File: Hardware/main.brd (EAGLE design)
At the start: 100 x 49.2 mm, 40 parts, among them IC3 MEGA128-A, K1 DS2-L2-12V, T1 IRML5202, T2 IRML5202, T3 IRML5202, T4 IRML5202, U1 DS1307ZN+

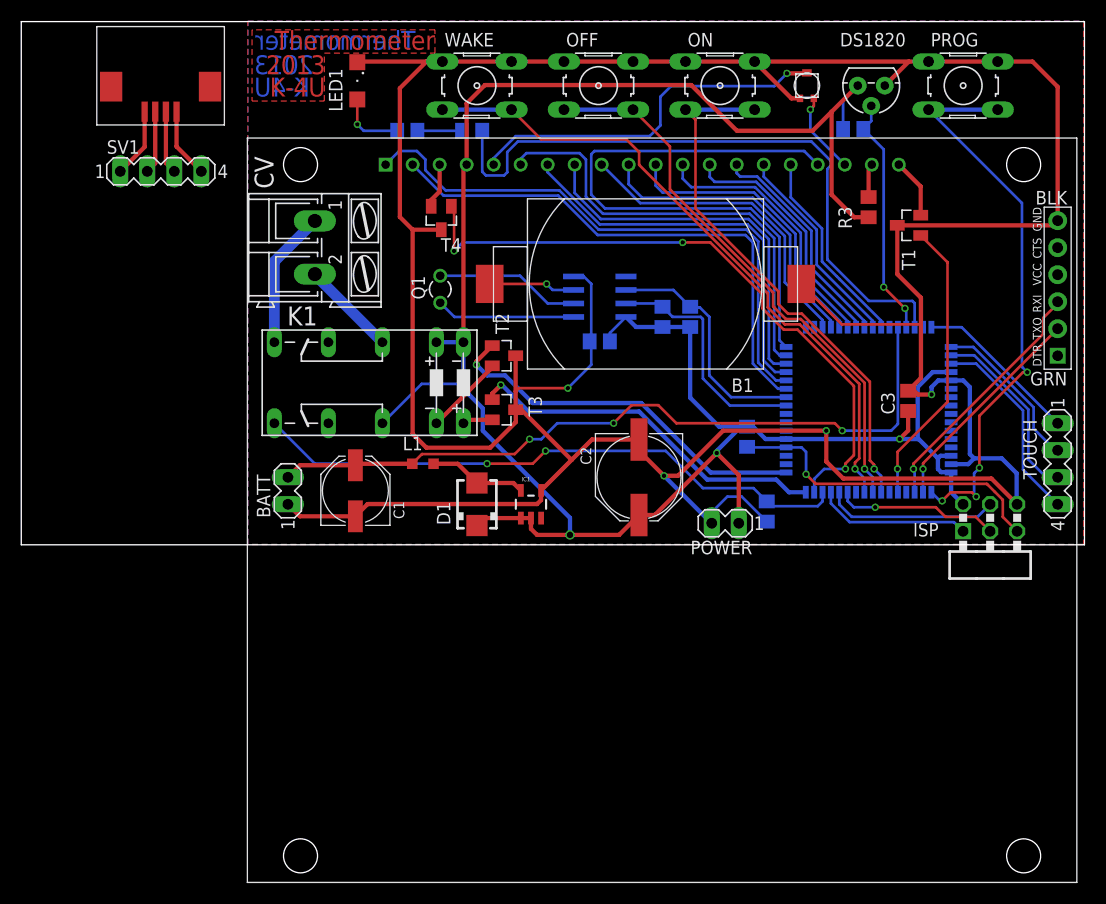
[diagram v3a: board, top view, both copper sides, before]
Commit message: Presets added, time added, CV added
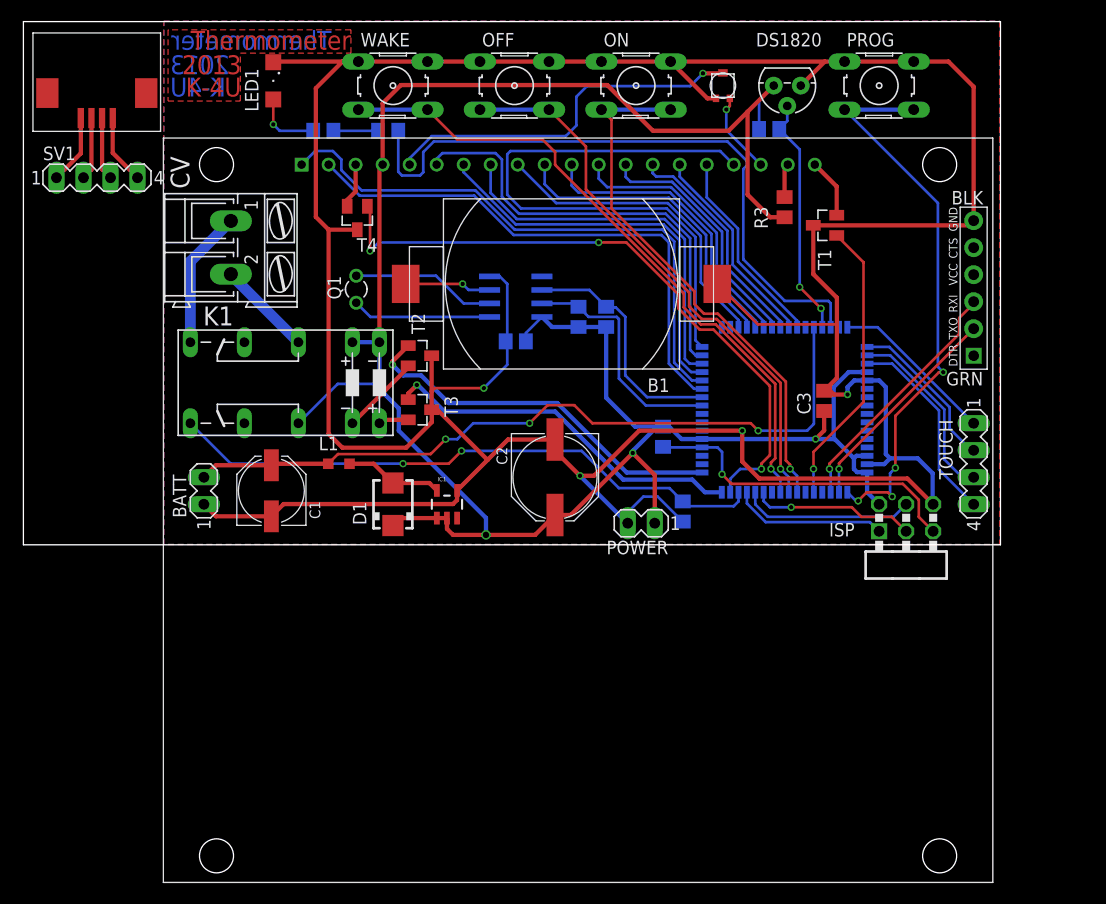
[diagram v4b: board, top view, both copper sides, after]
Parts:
- moved C3 7.90 mm to (75.3, 13.6)
- moved C4 7.90 mm to (46.3, 19.2)
- moved DS1820 7.90 mm to (71.8, 43.2)
- moved IC3 7.90 mm to (71.6, 12.8)
- moved JP2 7.90 mm to (89.4, 24.2)
- moved ON 7.90 mm to (57.6, 43.2)
- moved PROG 7.90 mm to (80.5, 43.2)
- moved R2 7.90 mm to (70.1, 39.2)
- moved R3 7.90 mm to (71.6, 31.8)
- moved R4 7.90 mm to (65.8, 43.2)
- moved R6 7.90 mm to (54.8, 21.5)
- moved R7 7.90 mm to (34.3, 39.0)
- moved R9 7.90 mm to (62.0, 3.20)
- moved T1 7.90 mm to (75.4, 30.1)
- moved TOUCH 7.90 mm to (89.4, 7.69)
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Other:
- board size 100 x 49.2 mm -> 91.9 x 49.2 mm

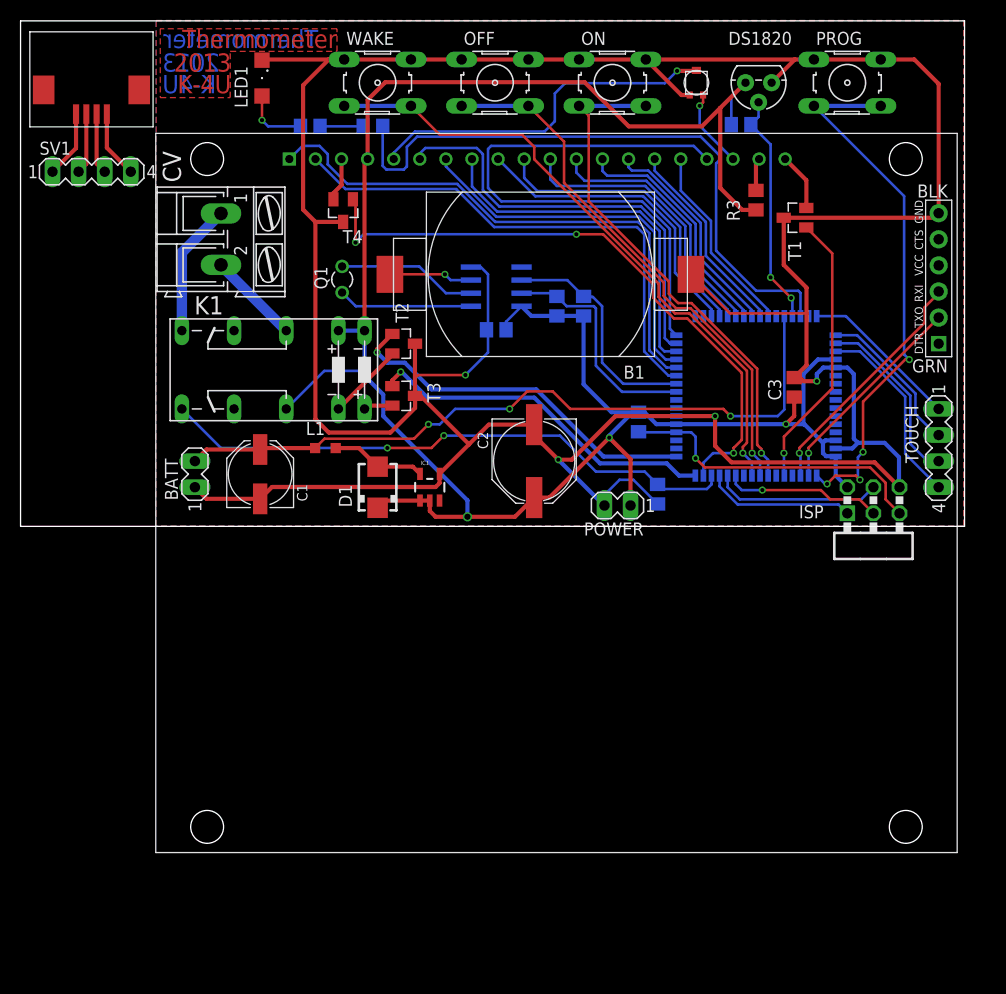
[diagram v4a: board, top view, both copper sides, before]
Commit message: Added some extra components + bigger PCB
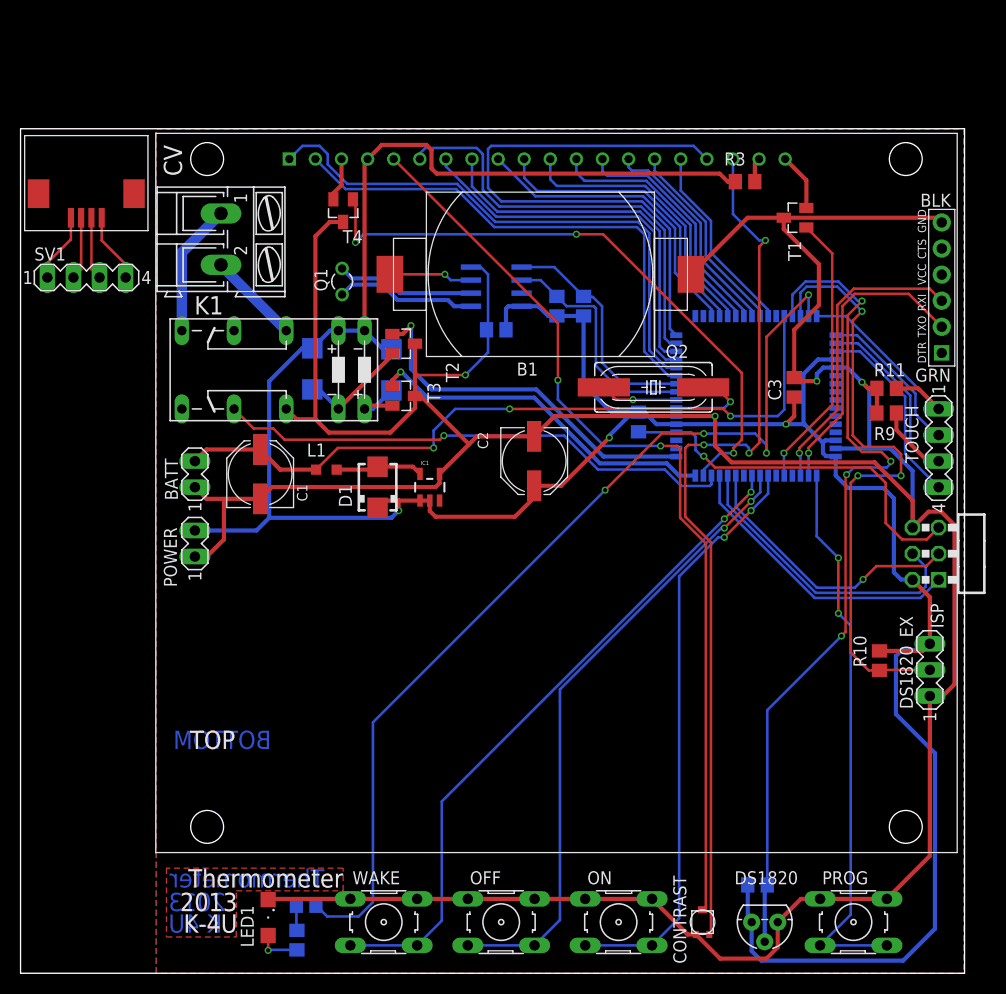
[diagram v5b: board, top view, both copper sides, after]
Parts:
- added D2, D3: MBRA340T3, diode:SMA
- added DS1820_EX: (no value), con-lstb:MA03-1
- added Q2: (no value), crystal:SM49
- added R10: 4k7, rcl:R0805
- added R11: 150, rcl:R0805
- C2: device rcl:PANASONIC_F -> rcl:PANASONIC_D
- R9: value 10K -> 150
- moved DS1820 81.7 mm to (72.4, -38.5)
- moved LED1 81.7 mm to (24.1, -38.0)
- moved OFF 81.7 mm to (46.8, -38.5)
- moved ON 81.7 mm to (58.2, -38.5)
- moved PROG 81.7 mm to (81.1, -38.5)
- moved R4 81.7 mm to (66.4, -38.5)
- moved WAKE 81.7 mm to (35.4, -38.5)
- moved R8 79.2 mm to (26.9, -40.2), turned to 270 degrees
- moved R7 76.1 mm to (27.8, -36.8)
- moved R2 74.0 mm to (71.7, -34.8)
- moved POWER 41.3 mm to (17.0, -1.60), turned to 90 degrees
- moved R9 23.7 mm to (84.3, 11.1), flipped to the top, turned to 0 degrees
- moved SV1 10.3 mm to (6.42, 24.3)
- moved U$1 10.1 mm to (7.90, 30.1)
- moved ISP 7.27 mm to (88.1, -2.59), turned to 90 degrees
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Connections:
- new net DS18B20_EX: DS1820_EX.2, IC3.46, R10.1
- new net N$33: IC3.23, Q2.2
- new net N$34: IC3.24, Q2.1
- net +5V: now also D2.C, D3.C, DS1820_EX.3, POWER.2, R10.2; no longer K1.P2, POWER.1
- net CV_ON: now also K1.O2; no longer K1.S2, R9.2
- net GND: now also DS1820_EX.1, K1.P2, POWER.1, R11.1; no longer POWER.2
- net N$14: now also D2.A
- net N$15: now also D3.A
- net N$20: now also R9.2
- net N$22: now also R11.2
- net N$30: now also IC3.47; no longer IC3.46
- net SCL: now also U1.6; no longer U1.7
- net SDA: now also U1.5; no longer U1.6
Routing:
- net N$12: track 7.71 -> 86.3 mm, vias 1 -> 3
- net +5V: track 213.5 -> 282.8 mm
- net DS18B20: track 22.8 -> 82.9 mm, vias 2 -> 4
- net DS18B20_EX: track 0.00 -> 59.7 mm, vias 0 -> 3
- net N$13: track 35.0 -> 89.9 mm, vias 1 -> 2
- net N$30: track 61.5 -> 94.5 mm, vias 0 -> 4
- net MISO: track 14.6 -> 28.5 mm
- net MOSI: track 16.3 -> 29.7 mm
- net SCK: track 15.4 -> 27.4 mm
- net GND: track 339.6 -> 350.9 mm
- net N$16: track 52.6 -> 61.5 mm, vias 1 -> 2
- net N$33: track 0.00 -> 8.79 mm, vias 0 -> 1
- net N$11: track 20.6 -> 29.3 mm
- net N$34: track 0.00 -> 7.55 mm, vias 0 -> 1
- net N$20: track 17.5 -> 24.5 mm
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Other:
- board size 91.9 x 49.2 mm -> 91.9 x 82.2 mm
- board text added: "BOTTOM"
- board text added: "CONTRAST"
- board text added: "TOP"

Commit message: This pcb version has been send to seeed.
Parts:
- added RESET: (no value), switch-omron:B3F-10XX
- PROG: value (none) -> MA02-1; device switch-omron:B3F-10XX -> con-lstb:MA02-1
- T1, T2, T3, T4: value IRML5202 -> IRLML2502PBF
- moved B1 40.2 mm to (42.9, -14.9)
- moved PROG 17.9 mm to (88.6, -22.2), turned to 90 degrees
- moved Q1 8.32 mm to (39.4, 22.0)
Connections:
- net !RESET: now also RESET.3, RESET.4
- net GND: now also RESET.1, RESET.2; no longer PROG.2
- net N$8: now also PROG.2; no longer PROG.3, PROG.4
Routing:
- net !RESET: track 37.1 -> 91.9 mm, vias 1 -> 2
- net GND: track 350.9 -> 395.0 mm
- net N$24: track 8.12 -> 51.8 mm, vias 1 -> 3
- net N$8: track 55.0 -> 33.3 mm, vias 2 -> 1
- net N$26: track 13.8 -> 4.75 mm
- net N$27: track 13.5 -> 4.65 mm
- net DS18B20: track 82.9 -> 86.4 mm

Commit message: New programming header
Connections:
- removed net MISO: IC3.13, ISP.1
- removed net MOSI: IC3.12, ISP.4
- removed net N$11: IC3.2, JP2.P$2
- removed net N$2: IC3.3, JP2.P$3
- new net PDI: IC3.2, ISP.4, JP2.P$2
- new net PDO: IC3.3, ISP.1, JP2.P$3
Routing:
- net PDI: track 0.00 -> 50.8 mm, vias 0 -> 1
- net PDO: track 0.00 -> 49.8 mm, vias 0 -> 1
- net MOSI: track 29.7 -> 0.00 mm
- net N$2: track 29.5 -> 0.00 mm, vias 1 -> 0
- net N$11: track 29.3 -> 0.00 mm, vias 1 -> 0
- net MISO: track 28.5 -> 0.00 mm
- net SCK: track 27.4 -> 31.9 mm, vias 1 -> 2
- net N$28: track 57.3 -> 56.9 mm, vias 2 -> 0
- net N$16: track 61.5 -> 61.3 mm, vias 2 -> 0
- net N$10: vias 2 -> 0
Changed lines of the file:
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@@
 <wire x1="38.6012" y1="-40.7106" x2="41" y2="-38.3118" width="0.254" layer="16"/>
 <wire x1="41" y1="-38.3118" x2="41" y2="-26.7" width="0.254" layer="16"/>
-<via x="68.5" y="0.8" extent="1-16" drill="0.4"/>
-<via x="71.1" y="3.4" extent="1-16" drill="0.4"/>
-<wire x1="71.1" y1="3.4" x2="71.1863" y2="3.4863" width="0.254" layer="16"/>
 <wire x1="71.1863" y1="3.4863" x2="71.1863" y2="5.0103" width="0.254" layer="16"/>
-<wire x1="71.1" y1="3.4" x2="68.5" y2="0.8" width="0.254" layer="1"/>
-<wire x1="68.5" y1="0.8" x2="41" y2="-26.7" width="0.254" layer="16"/>
-</signal>
-<signal name="MOSI">
-<contactref element="ISP" pad="4"/>
-<contactref element="IC3" pad="12"/>
-<wire x1="87.5" y1="-6.4" x2="88.1" y2="-5.8" width="0.254" layer="16"/>
-<wire x1="88.1" y1="-5.8" x2="88.1" y2="-3.87" width="0.254" layer="16"/>
-<wire x1="88.1" y1="-3.87" x2="86.82" y2="-2.59" width="0.254" layer="16"/>
-<wire x1="87.5" y1="-6.4" x2="77.4" y2="-6.4" width="0.254" layer="16"/>
-<wire x1="68.8241" y1="2.1759" x2="68.8241" y2="5.0103" width="0.254" layer="16"/>
-<wire x1="77.4" y1="-6.4" x2="68.8241" y2="2.1759" width="0.254" layer="16"/>
-</signal>
-<signal name="MISO">
-<contactref element="ISP" pad="1"/>
-<contactref element="IC3" pad="13"/>
-<wire x1="87.59" y1="-6.9" x2="89.36" y2="-5.13" width="0.254" layer="16"/>
-<wire x1="68.0367" y1="5.0103" x2="68.0367" y2="2.3633" width="0.254" layer="16"/>
-<wire x1="77.3" y1="-6.9" x2="87.59" y2="-6.9" width="0.254" layer="16"/>
-<wire x1="68.0367" y1="2.3633" x2="77.3" y2="-6.9" width="0.254" layer="16"/>
+<wire x1="71.1863" y1="3.4863" x2="41" y2="-26.7" width="0.254" layer="16"/>
 </signal>
 <signal name="SCK">
 <contactref element="ISP" pad="3"/>
 <contactref element="IC3" pad="11"/>
-<wire x1="83.3" y1="-3.8" x2="88.15" y2="-3.8" width="0.254" layer="1"/>
-<wire x1="88.15" y1="-3.8" x2="89.36" y2="-2.59" width="0.254" layer="1"/>
-<wire x1="69.6115" y1="5.0103" x2="69.6115" y2="1.9885" width="0.254" layer="16"/>
-<wire x1="77.5" y1="-5.9" x2="81.2" y2="-5.9" width="0.254" layer="16"/>
-<wire x1="81.2" y1="-5.9" x2="82" y2="-5.1" width="0.254" layer="16"/>
-<via x="82" y="-5.1" extent="1-16" drill="0.4"/>
-<wire x1="82" y1="-5.1" x2="83.3" y2="-3.8" width="0.254" layer="1"/>
-<wire x1="69.6115" y1="1.9885" x2="77.5" y2="-5.9" width="0.254" layer="16"/>
+<wire x1="69.6115" y1="5.0103" x2="69.6115" y2="3.2885" width="0.254" layer="16"/>
+<wire x1="69.6115" y1="3.2885" x2="69.7" y2="3.2" width="0.254" layer="16"/>
+<via x="69.7" y="3.2" extent="1-16" drill="0.4"/>
+<wire x1="69.7" y1="3.2" x2="71.4" y2="1.5" width="0.254" layer="1"/>
+<via x="71.4" y="1.5" extent="1-16" drill="0.4"/>
+<wire x1="71.4" y1="1.5" x2="76.8" y2="1.5" width="0.254" layer="16"/>
+<wire x1="76.8" y1="1.5" x2="85.7" y2="-7.4" width="0.254" layer="16"/>
+<wire x1="85.7" y1="-7.4" x2="89.4" y2="-7.4" width="0.254" layer="16"/>
+<wire x1="89.4" y1="-7.4" x2="90.5" y2="-6.3" width="0.254" layer="16"/>
+<wire x1="90.5" y1="-6.3" x2="90.5" y2="-3.4" width="0.254" layer="16"/>
+<wire x1="90.5" y1="-3.4" x2="89.69" y2="-2.59" width="0.254" layer="16"/>
+<wire x1="89.69" y1="-2.59" x2="89.36" y2="-2.59" width="0.254" layer="16"/>
 </signal>
 <signal name="!RESET">
@@
 <wire x1="74.3" y1="7.2" x2="79" y2="11.9" width="0.254" layer="1"/>
 </signal>
-<signal name="N$2">
+<signal name="PDO">
 <contactref element="JP2" pad="P$3"/>
 <contactref element="IC3" pad="3"/>
@@
 <wire x1="88.49" y1="23.2" x2="81.1" y2="23.2" width="0.254" layer="1"/>
 <wire x1="81.1" y1="23.2" x2="79.5" y2="21.6" width="0.254" layer="1"/>
-</signal>
-<signal name="N$11">
+<contactref element="ISP" pad="1"/>
+<wire x1="87.59" y1="-6.9" x2="89.36" y2="-5.13" width="0.254" layer="16"/>
+<wire x1="75.9107" y1="5.0103" x2="75.9107" y2="2.9893" width="0.254" layer="16"/>
+<wire x1="75.9107" y1="2.9893" x2="85.8" y2="-6.9" width="0.254" layer="16"/>
+<wire x1="85.8" y1="-6.9" x2="87.59" y2="-6.9" width="0.254" layer="16"/>
+</signal>
+<signal name="PDI">
 <contactref element="IC3" pad="2"/>
 <contactref element="JP2" pad="P$2"/>
@@
 <wire x1="81.2" y1="22.7" x2="80" y2="21.5" width="0.254" layer="1"/>
 <wire x1="80" y1="21.5" x2="80" y2="11.03" width="0.254" layer="1"/>
+<contactref element="ISP" pad="4"/>
+<wire x1="87.5" y1="-6.4" x2="88.1" y2="-5.8" width="0.254" layer="16"/>
+<wire x1="88.1" y1="-5.8" x2="88.1" y2="-3.87" width="0.254" layer="16"/>
+<wire x1="88.1" y1="-3.87" x2="86.82" y2="-2.59" width="0.254" layer="16"/>
+<wire x1="87.5" y1="-6.4" x2="85.9" y2="-6.4" width="0.254" layer="16"/>
+<wire x1="85.9" y1="-6.4" x2="76.6981" y2="2.8019" width="0.254" layer="16"/>
+<wire x1="76.6981" y1="2.8019" x2="76.6981" y2="5.0103" width="0.254" layer="16"/>
 </signal>
 <signal name="DS18B20">
@@
 <wire x1="43.5288" y1="-40.7106" x2="50.0312" y2="-40.7106" width="0.254" layer="16"/>
 <wire x1="50.0312" y1="-40.7106" x2="52.5" y2="-38.2418" width="0.254" layer="16"/>
-<wire x1="52.5" y1="-38.2418" x2="52.5" y2="-16.9" width="0.254" layer="16"/>
-<via x="71.1" y="2.5" extent="1-16" drill="0.4"/>
-<wire x1="52.5" y1="-16.9" x2="52.5" y2="-16.1" width="0.254" layer="16"/>
+<wire x1="52.5" y1="-38.2418" x2="52.5" y2="-15.8" width="0.254" layer="16"/>
 <wire x1="72" y1="4.984" x2="71.9737" y2="5.0103" width="0.254" layer="16"/>
-<wire x1="71.1" y1="2.5" x2="68.5" y2="-0.1" width="0.254" layer="1"/>
-<via x="68.5" y="-0.1" extent="1-16" drill="0.4"/>
-<wire x1="72" y1="4.984" x2="72" y2="3.4" width="0.254" layer="16"/>
-<wire x1="72" y1="3.4" x2="71.1" y2="2.5" width="0.254" layer="16"/>
-<wire x1="68.5" y1="-0.1" x2="68.2" y2="-0.1" width="0.254" layer="16"/>
-<wire x1="68.2" y1="-0.1" x2="52.5" y2="-15.8" width="0.254" layer="16"/>
-<wire x1="52.5" y1="-15.8" x2="52.5" y2="-16.1" width="0.254" layer="16"/>
+<wire x1="72" y1="4.984" x2="72" y2="3.7" width="0.254" layer="16"/>
+<wire x1="72" y1="3.7" x2="52.5" y2="-15.8" width="0.254" layer="16"/>
 </signal>
 <signal name="N$17">
@@
 <wire x1="61.4612" y1="-40.7106" x2="64.1" y2="-38.0718" width="0.254" layer="16"/>
 <wire x1="64.1" y1="-38.0718" x2="64.1" y2="-4.8" width="0.254" layer="16"/>
-<via x="68.5" y="-1" extent="1-16" drill="0.4"/>
-<via x="71.1" y="1.6" extent="1-16" drill="0.4"/>
-<wire x1="72.7611" y1="5.0103" x2="72.7611" y2="3.2611" width="0.254" layer="16"/>
-<wire x1="72.7611" y1="3.2611" x2="71.1" y2="1.6" width="0.254" layer="16"/>
-<wire x1="71.1" y1="1.6" x2="68.5" y2="-1" width="0.254" layer="1"/>
-<wire x1="68.5" y1="-1" x2="67.9" y2="-1" width="0.254" layer="16"/>
-<wire x1="67.9" y1="-1" x2="64.1" y2="-4.8" width="0.254" layer="16"/>
+<wire x1="64.1" y1="-4.8" x2="72.7611" y2="3.8611" width="0.254" layer="16"/>
+<wire x1="72.7611" y1="3.8611" x2="72.7611" y2="5.0103" width="0.254" layer="16"/>
 </signal>
 <signal name="N$30">
